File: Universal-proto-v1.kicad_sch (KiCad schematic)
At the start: 45 parts, among them J1 Bus_ISA_8bit, J2 ISA Breakout, J3 Pico GPIO Breakout 2, J4 Pico GPIO Breakout 1

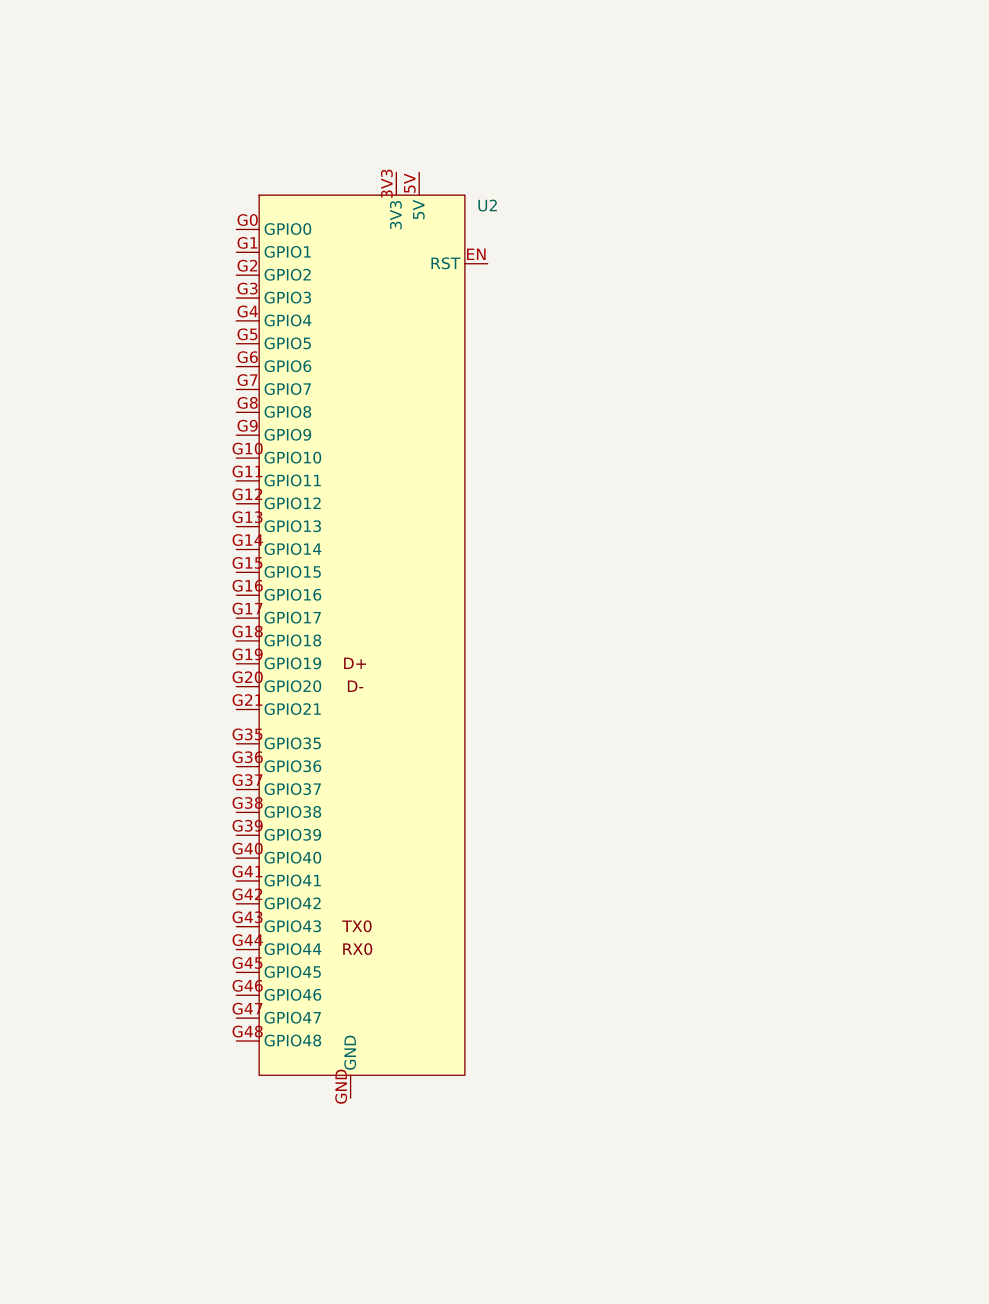
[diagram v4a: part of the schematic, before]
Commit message: Added logos
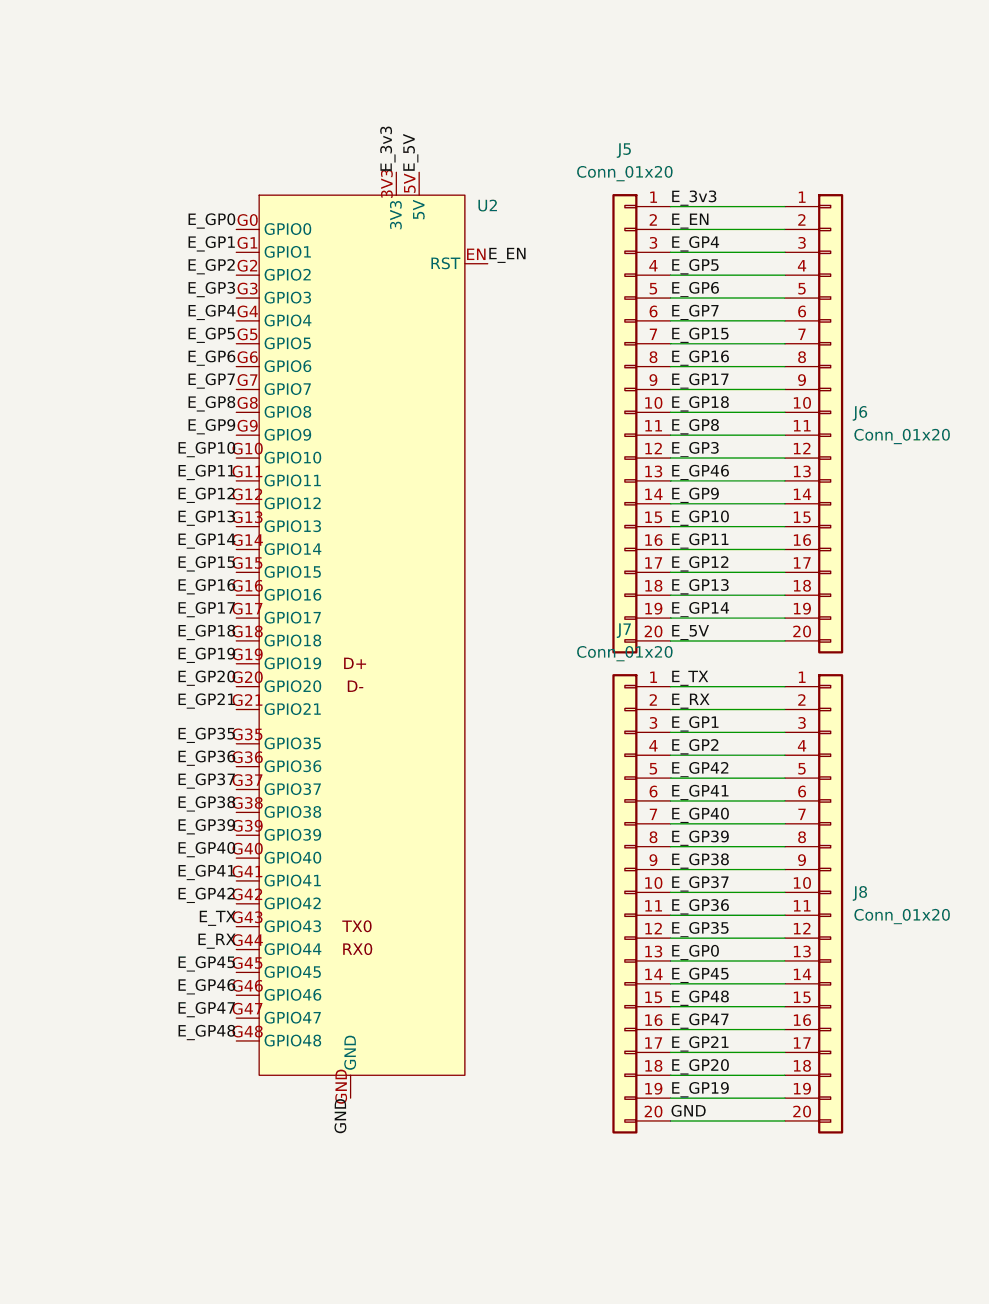
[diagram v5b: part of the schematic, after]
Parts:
- added J5, J6, J7, J8: Conn_01x20, Connector_PinHeader_2.54mm:PinHeader_1x20_P2.54mm_Vertical, symbol Connector_Generic:Conn_01x20
- J1: footprint Connector_PCBEdge:BUS_AT -> parts:ISA_8bit
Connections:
- net GND: now also U2.GND, J7.20 (Pin_20), J8.20 (Pin_20)
- net E_3v3: now reaches U2.3V3
- net E_3v3: now also J5.1 (Pin_1), J6.1 (Pin_1)
- net E_5V: now reaches U2.5V
- net E_5V: now also J5.20 (Pin_20), J6.20 (Pin_20)
- net E_EN: now reaches U2.EN (RST)
- net E_EN: now also J5.2 (Pin_2), J6.2 (Pin_2)
- net E_GP0: now reaches U2.G0 (GPIO0)
- net E_GP0: now also J7.13 (Pin_13), J8.13 (Pin_13)
- net E_GP1: now reaches U2.G1 (GPIO1)
- net E_GP1: now also J7.3 (Pin_3), J8.3 (Pin_3)
- net E_GP10: now reaches U2.G10 (GPIO10)
- net E_GP10: now also J5.15 (Pin_15), J6.15 (Pin_15)
- net E_GP11: now reaches U2.G11 (GPIO11)
- net E_GP11: now also J5.16 (Pin_16), J6.16 (Pin_16)
- net E_GP12: now reaches U2.G12 (GPIO12)
- net E_GP12: now also J5.17 (Pin_17), J6.17 (Pin_17)
- net E_GP13: now reaches U2.G13 (GPIO13)
- net E_GP13: now also J5.18 (Pin_18), J6.18 (Pin_18)
- net E_GP14: now reaches U2.G14 (GPIO14)
- net E_GP14: now also J5.19 (Pin_19), J6.19 (Pin_19)
- net E_GP15: now reaches U2.G15 (GPIO15)
- net E_GP15: now also J5.7 (Pin_7), J6.7 (Pin_7)
- net E_GP16: now reaches U2.G16 (GPIO16)
- net E_GP16: now also J5.8 (Pin_8), J6.8 (Pin_8)
- net E_GP17: now reaches U2.G17 (GPIO17)
- net E_GP17: now also J5.9 (Pin_9), J6.9 (Pin_9)
- net E_GP18: now reaches U2.G18 (GPIO18)
- net E_GP18: now also J5.10 (Pin_10), J6.10 (Pin_10)
- net E_GP19: now reaches U2.G19 (GPIO19)
- net E_GP19: now also J7.19 (Pin_19), J8.19 (Pin_19)
- net E_GP2: now reaches U2.G2 (GPIO2)
- net E_GP2: now also J7.4 (Pin_4), J8.4 (Pin_4)
- net E_GP20: now reaches U2.G20 (GPIO20)
- net E_GP20: now also J7.18 (Pin_18), J8.18 (Pin_18)
- net E_GP21: now reaches U2.G21 (GPIO21)
- net E_GP21: now also J7.17 (Pin_17), J8.17 (Pin_17)
- net E_GP3: now reaches U2.G3 (GPIO3)
- net E_GP3: now also J5.12 (Pin_12), J6.12 (Pin_12)
- net E_GP35: now reaches U2.G35 (GPIO35)
- net E_GP35: now also J7.12 (Pin_12), J8.12 (Pin_12)
- net E_GP36: now reaches U2.G36 (GPIO36)
- net E_GP36: now also J7.11 (Pin_11), J8.11 (Pin_11)
- net E_GP37: now reaches U2.G37 (GPIO37)
- net E_GP37: now also J7.10 (Pin_10), J8.10 (Pin_10)
- net E_GP38: now reaches U2.G38 (GPIO38)
- net E_GP38: now also J7.9 (Pin_9), J8.9 (Pin_9)
- net E_GP39: now reaches U2.G39 (GPIO39)
- net E_GP39: now also J7.8 (Pin_8), J8.8 (Pin_8)
- net E_GP4: now reaches U2.G4 (GPIO4)
- net E_GP4: now also J5.3 (Pin_3), J6.3 (Pin_3)
- net E_GP40: now reaches U2.G40 (GPIO40)
- net E_GP40: now also J7.7 (Pin_7), J8.7 (Pin_7)
- net E_GP41: now reaches U2.G41 (GPIO41)
- net E_GP41: now also J7.6 (Pin_6), J8.6 (Pin_6)
- net E_GP42: now reaches U2.G42 (GPIO42)
- net E_GP42: now also J7.5 (Pin_5), J8.5 (Pin_5)
- net E_TX: now reaches U2.G43 (GPIO43)
- net E_TX: now also J7.1 (Pin_1), J8.1 (Pin_1)
- net E_RX: now reaches U2.G44 (GPIO44)
- net E_RX: now also J7.2 (Pin_2), J8.2 (Pin_2)
- net E_GP45: now reaches U2.G45 (GPIO45)
- net E_GP45: now also J7.14 (Pin_14), J8.14 (Pin_14)
- net E_GP46: now reaches U2.G46 (GPIO46)
- net E_GP46: now also J5.13 (Pin_13), J6.13 (Pin_13)
- net E_GP47: now reaches U2.G47 (GPIO47)
- net E_GP47: now also J7.16 (Pin_16), J8.16 (Pin_16)
- net E_GP48: now reaches U2.G48 (GPIO48)
- net E_GP48: now also J7.15 (Pin_15), J8.15 (Pin_15)
- net E_GP5: now reaches U2.G5 (GPIO5)
- net E_GP5: now also J5.4 (Pin_4), J6.4 (Pin_4)
- net E_GP6: now reaches U2.G6 (GPIO6)
- net E_GP6: now also J5.5 (Pin_5), J6.5 (Pin_5)
- net E_GP7: now reaches U2.G7 (GPIO7)
- net E_GP7: now also J5.6 (Pin_6), J6.6 (Pin_6)
- net E_GP8: now reaches U2.G8 (GPIO8)
- net E_GP8: now also J5.11 (Pin_11), J6.11 (Pin_11)
- net E_GP9: now reaches U2.G9 (GPIO9)
- net E_GP9: now also J5.14 (Pin_14), J6.14 (Pin_14)

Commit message: Added warning, diode, jumpers for 5V from edge
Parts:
- added D1: D, Diode_THT:D_DO-15_P15.24mm_Horizontal, symbol Device:D
- added J9: Conn_02x02_Odd_Even, Connector_PinHeader_2.54mm:PinHeader_2x02_P2.54mm_Vertical, symbol Connector_Generic:Conn_02x02_Odd_Even
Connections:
- net E_5V: now also J9.4 (Pin_4)
- net VBUS: now also J9.2 (Pin_2)
- net VCC: now also D1.2 (A)
- new net: D1.1 (K), J9.1 (Pin_1), J9.3 (Pin_3)
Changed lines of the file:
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@@
 		(members "A[0..19]" "GP[0..19]")
 	)
+	(junction
+		(at 20.32 114.3)
+		(diameter 0)
+		(color 0 0 0 0)
+	)
 	(no_connect
 		(at 182.88 20.32)
@@
 	(wire
 		(pts
+			(xy 20.32 101.6) (xy 31.75 101.6)
+		)
+		(stroke
+			(width 0)
+			(type default)
+		)
+	)
+	(wire
+		(pts
 			(xy 153.67 57.15) (xy 172.72 57.15)
 		)
@@
 	(wire
 		(pts
+			(xy 20.32 109.22) (xy 20.32 114.3)
+		)
+		(stroke
+			(width 0)
+			(type default)
+		)
+	)
+	(wire
+		(pts
 			(xy 153.67 118.11) (xy 172.72 118.11)
 		)
@@
 	(wire
 		(pts
+			(xy 20.32 114.3) (xy 20.32 116.84)
+		)
+		(stroke
+			(width 0)
+			(type default)
+		)
+	)
+	(wire
+		(pts
 			(xy 146.05 97.79) (xy 140.97 97.79)
 		)
@@
 		)
 	)
+	(label "E_5V"
+		(at 33.02 116.84 0)
+		(effects
+			(font
+				(size 1.27 1.27)
+			)
+			(justify left bottom)
+		)
+	)
 	(label "BA05"
 		(at 116.84 41.91 0)
@@
 		)
 	)
+	(label "VBUS"
+		(at 33.02 114.3 0)
+		(effects
+			(font
+				(size 1.27 1.27)
+			)
+			(justify left bottom)
+		)
+	)
 	(label "E_GP14"
 		(at 311.15 73.66 180)
@@
 	)
 	(symbol
+		(lib_id "Device:D")
+		(at 20.32 105.41 90)
+		(unit 1)
+		(exclude_from_sim no)
+		(in_bom yes)
+		(on_board yes)
+		(dnp no)
+		(fields_autoplaced yes)
+		(property "Reference" "D1"
+			(at 22.86 104.1399 90)
+			(effects
+				(font
+					(size 1.27 1.27)
+				)
+				(justify right)
+			)
+		)
+		(property "Value" "D"
+			(at 22.86 106.6799 90)
+			(effects
+				(font
+					(size 1.27 1.27)
+				)
+				(justify right)
+			)
+		)
+		(property "Footprint" "Diode_THT:D_DO-15_P15.24mm_Horizontal"
+			(at 20.32 105.41 0)
+			(effects
+				(font
+					(size 1.27 1.27)
+				)
+				(hide yes)
+			)
+		)
+		(property "Datasheet" "~"
+			(at 20.32 105.41 0)
+			(effects
+				(font
+					(size 1.27 1.27)
+				)
+				(hide yes)
+			)
+		)
+		(property "Description" "Diode"
+			(at 20.32 105.41 0)
+			(effects
+				(font
+					(size 1.27 1.27)
+				)
+				(hide yes)
+			)
+		)
+		(property "Sim.Device" "D"
+			(at 20.32 105.41 0)
+			(effects
+				(font
+					(size 1.27 1.27)
+				)
+				(hide yes)
+			)
+		)
+		(property "Sim.Pins" "1=K 2=A"
+			(at 20.32 105.41 0)
+			(effects
+				(font
+					(size 1.27 1.27)
+				)
+				(hide yes)
+			)
+		)
+		(pin "2"
+		)
+		(pin "1"
+		)
+		(instances
+			(project ""
+				(path "/14d49e36-dbe1-431d-b439-c2a0c8a95850"
+					(reference "D1")
+					(unit 1)
+				)
+			)
+		)
+	)
+	(symbol
 		(lib_id "power:PWR_FLAG")
 		(at 44.45 134.62 270)
@@
 					(unit 1)
 				)
+			)
+		)
+	)
+	(symbol
+		(lib_id "Connector_Generic:Conn_02x02_Odd_Even")
+		(at 25.4 114.3 0)
+		(unit 1)
+		(exclude_from_sim no)
+		(in_bom yes)
+		(on_board yes)
+		(dnp no)
+		(fields_autoplaced yes)
+		(property "Reference" "J9"
+			(at 26.67 107.95 0)
+			(effects
+				(font
+					(size 1.27 1.27)
+				)
+			)
+		)
+		(property "Value" "Conn_02x02_Odd_Even"
+			(at 26.67 110.49 0)
+			(effects
+				(font
+					(size 1.27 1.27)
+				)
+			)
+		)
+		(property "Footprint" "Connector_PinHeader_2.54mm:PinHeader_2x02_P2.54mm_Vertical"
+			(at 25.4 114.3 0)
+			(effects
+				(font
+					(size 1.27 1.27)
+				)
+				(hide yes)
+			)
+		)
+		(property "Datasheet" "~"
+			(at 25.4 114.3 0)
+			(effects
+				(font
+					(size 1.27 1.27)
+				)
+				(hide yes)
+			)
+		)
+		(property "Description" "Generic connector, double row, 02x02, odd/even pin numbering scheme (row 1 odd numbers, row 2 even numbers), script generated (kicad-library-utils/schlib/autogen/connector/)"
+			(at 25.4 114.3 0)
+			(effects
+				(font
+					(size 1.27 1.27)
+				)
+				(hide yes)
+			)
+		)
+		(pin "3"
+		)
+		(pin "1"
+		)
+		(pin "4"
+		)
+		(pin "2"
+		)
+		(instances
+			(project ""
+				(path "/14d49e36-dbe1-431d-b439-c2a0c8a95850"
+					(reference "J9")
+					(unit 1)
+				)
